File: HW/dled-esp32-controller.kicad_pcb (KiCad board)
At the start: 2 copper layers, 50 x 48 mm, 40 parts, among them J1 CS_4, J2 CS_3, J3 CS_2, J4 CS_2, J5 CS_3, J6 CS_5, J7 CS_3, J8 CS_Pwr, J9 CS_Pwr, Q1 STD46P4LLF6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

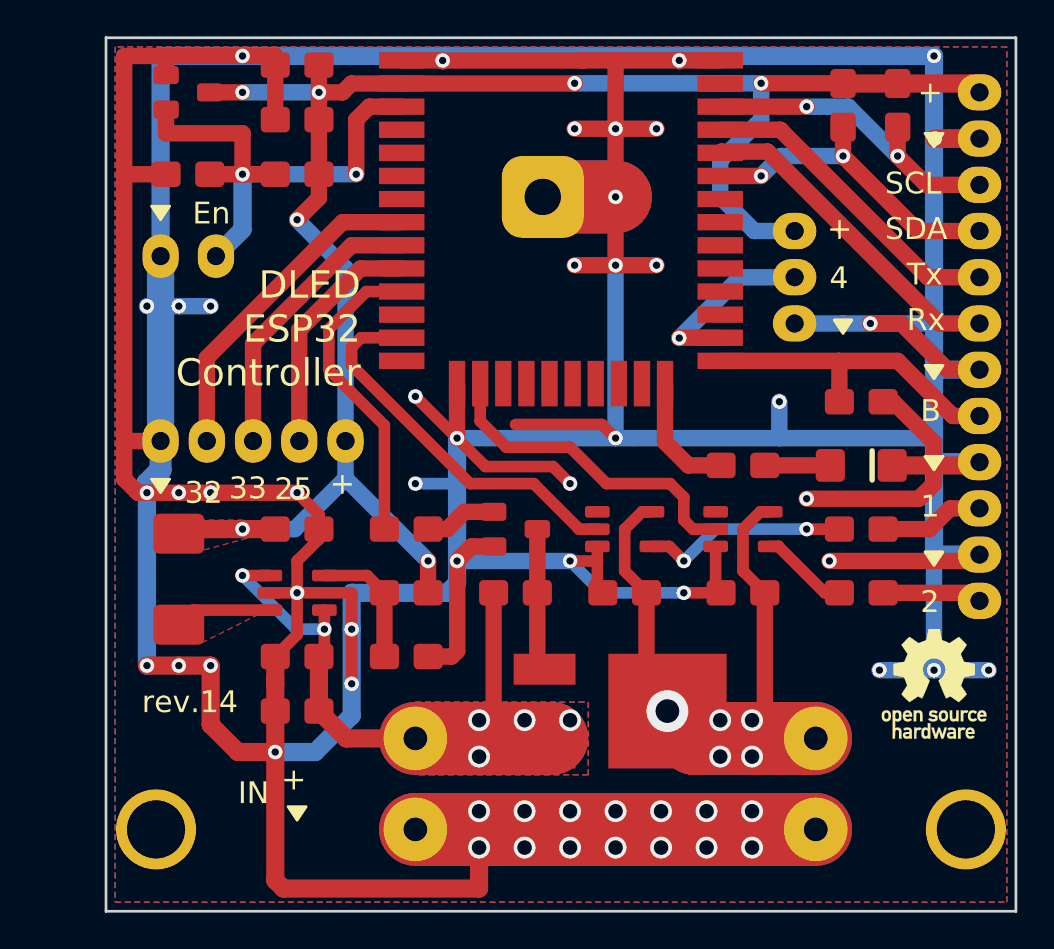
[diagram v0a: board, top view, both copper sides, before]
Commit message: Changes the C4 to NC and removes the keepout areas from under ESP32 module, as in Espressif's DevKitC v4
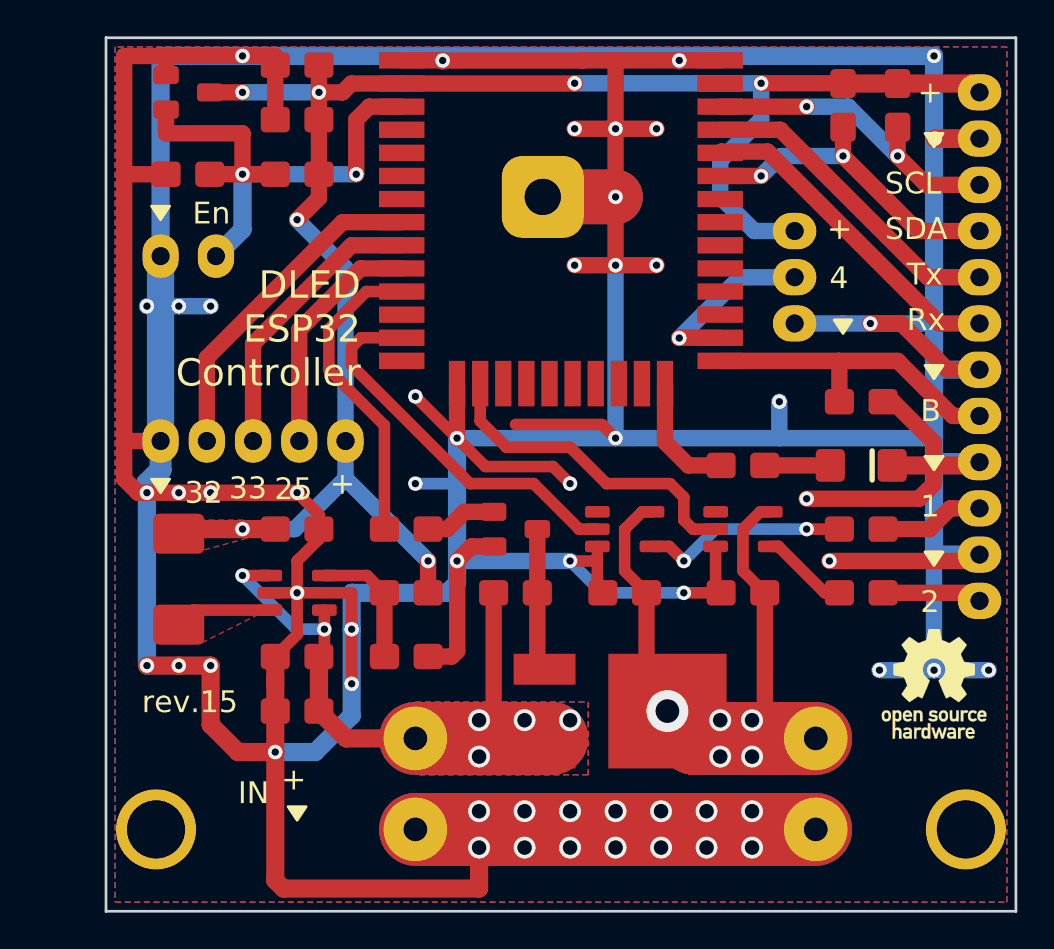
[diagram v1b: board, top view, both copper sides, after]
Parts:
- C4: value 100nF -> 100nF-NC
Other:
- board text added: "rev.15"
- board text removed: "rev.14"
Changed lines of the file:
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@@
       (effects (font (size 1 1) (thickness 0.15)))
     )
-    (fp_text value 100nF (at 0 -2) (layer F.Fab)
+    (fp_text value 100nF-NC (at 0 -2) (layer F.Fab)
       (effects (font (size 1 1) (thickness 0.15)))
     )
@@
     )
   )
-  (gr_text rev.14 (at 32.25 88.5) (layer F.SilkS)
+  (gr_text rev.15 (at 32.25 88.5) (layer F.SilkS)
     (effects (font (size 1.2 1.2) (thickness 0.25)) (justify right))
   )
@@
   (via (at 30.75 77) (size 0.8) (drill 0.4) (layers F.Cu B.Cu) (net 1))
   (segment (start 56.5 53.245) (end 53 53.245) (width 0.9) (layer F.Cu) (net 1))
-  (segment (start 49 60.745) (end 53 60.745) (width 4) (layer F.Cu) (net 1) (status 10))
-  (segment (start 49 60.745) (end 53 60.745) (width 4) (layer B.Cu) (net 1) (status 10))
+  (segment (start 49 60.745) (end 53 60.745) (width 3) (layer F.Cu) (net 1) (status 10))
+  (segment (start 49 60.745) (end 53 60.745) (width 3) (layer B.Cu) (net 1) (status 10))
   (via (at 53 60.745) (size 0.8) (drill 0.4) (layers F.Cu B.Cu) (net 1))
   (via (at 50.75 57) (size 0.8) (drill 0.4) (layers F.Cu B.Cu) (net 1))
@@
     )
   )
-  (zone (net 0) (net_name "") (layer F.Cu) (hatch edge 0.508)
-    (connect_pads no (clearance 0.8))
-    (min_thickness 0.5)
-    (keepout (tracks allowed) (vias allowed) (copperpour not_allowed))
-    (fill (arc_segments 16) (thermal_gap 0.5) (thermal_bridge_width 0.5))
-    (polygon
-      (pts
-        (xy 42.5 54.5) (xy 45 54.5) (xy 47 56.5) (xy 47 69) (xy 42.5 69)
-      )
-    )
-  )
   (zone (net 9) (net_name +5V) (layer F.Cu) (hatch edge 0.508)
     (priority 1)
@@
       )
     )
-  )
-  (zone (net 0) (net_name "") (layer B.Cu) (hatch edge 0.508)
-    (connect_pads no (clearance 0.8))
-    (min_thickness 0.5)
-    (keepout (tracks allowed) (vias allowed) (copperpour not_allowed))
-    (fill (arc_segments 16) (thermal_gap 0.5) (thermal_bridge_width 0.5))
-    (polygon
-      (pts
-        (xy 42.5 54.5) (xy 45 54.5) (xy 47 56.5) (xy 47 69) (xy 42.5 69)
-      )
-    )

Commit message: Improves component placement for ESP's power and reset circuitry.
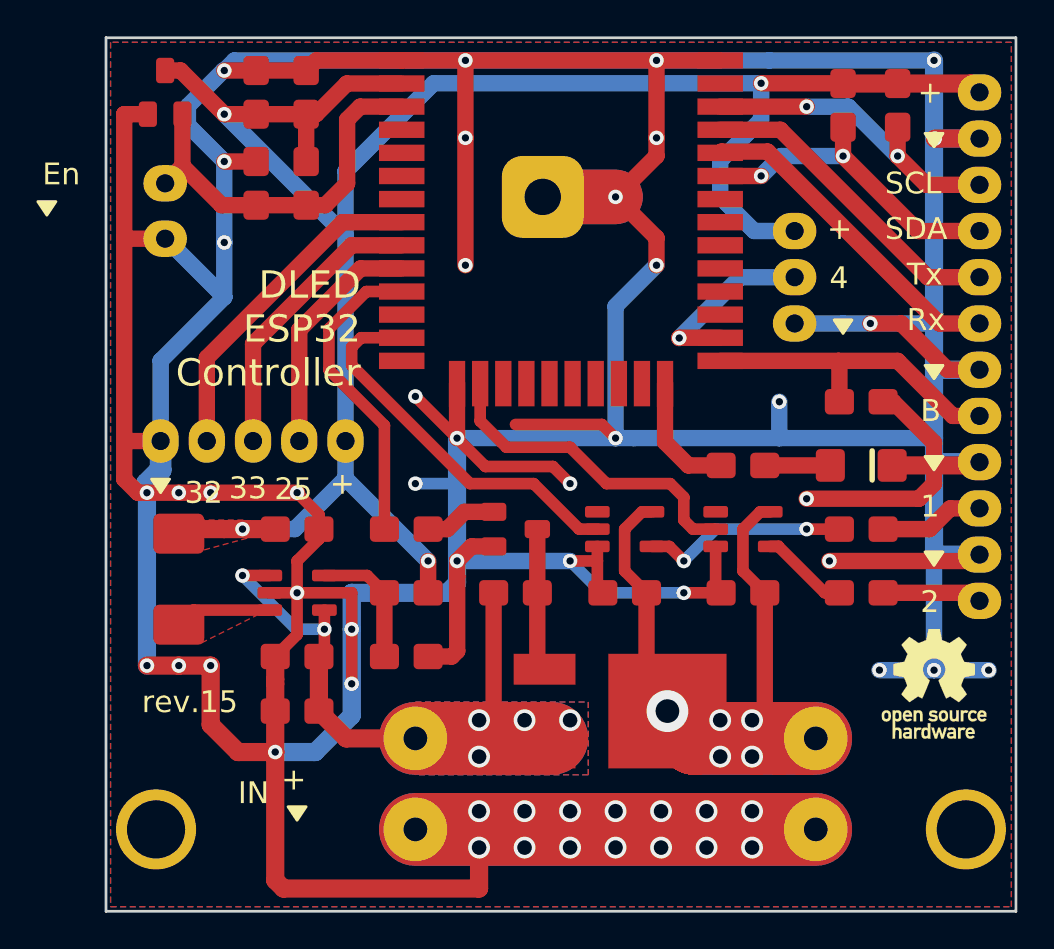
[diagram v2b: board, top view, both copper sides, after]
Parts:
- moved J4 4.88 mm to (28.2, 60.0), turned to 0 degrees
- moved C1 3.78 mm to (33.2, 60.0), turned to 90 degrees
- moved C3 2.70 mm to (33.2, 55.0), turned to 90 degrees
- moved C2 1.58 mm to (36.0, 55.0), turned to 90 degrees
- moved U2 1.25 mm to (28.2, 55.0), turned to 90 degrees
- moved R1 0.71 mm to (36.0, 60.0), turned to 270 degrees
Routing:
- net +3V3: track 99.5 -> 113.1 mm, vias 7 -> 4
- net /Reset: track 28.5 -> 21.4 mm, vias 2 -> 0
- net GND: track 486.9 -> 488.2 mm, vias 55 -> 52

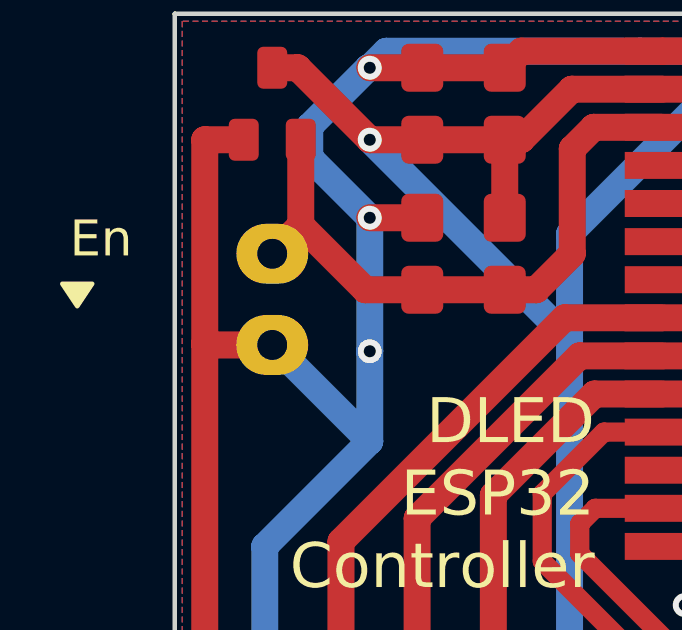
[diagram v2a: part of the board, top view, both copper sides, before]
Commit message: Creates the files for PCB fabrication, and adjusts the PCB layout a little.
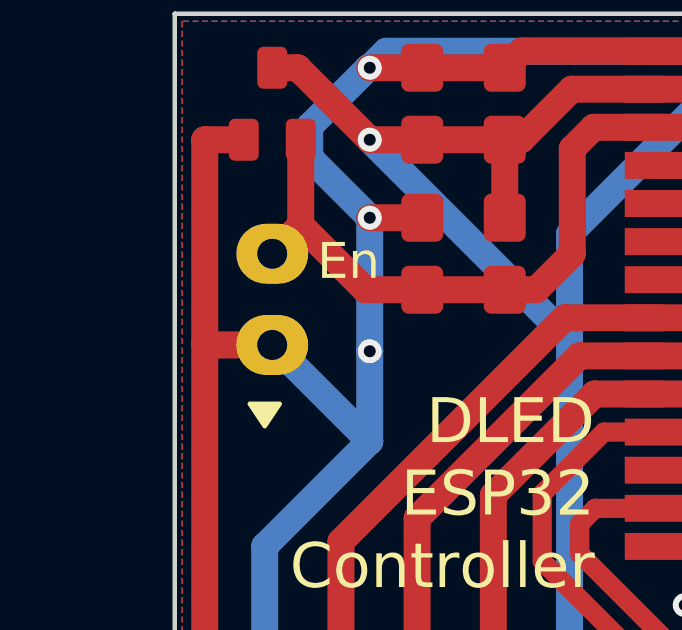
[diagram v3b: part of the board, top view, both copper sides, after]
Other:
- rule pad_to_mask_clearance: 0.051 -> 0.08
- rule solder_mask_min_width: 0.25 -> 0.35
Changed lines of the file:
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@@
   )
   (setup
-    (last_trace_width 0.9)
+    (last_trace_width 0.35)
     (user_trace_width 0.35)
     (user_trace_width 0.6)
@@
     (user_trace_width 4)
     (trace_clearance 0.3)
-    (zone_clearance 0.8)
+    (zone_clearance 0.7)
     (zone_45_only no)
     (trace_min 0.35)
@@
     (pad_size 3.5 3.5)
     (pad_drill 1.3)
-    (pad_to_mask_clearance 0.051)
-    (solder_mask_min_width 0.25)
+    (pad_to_mask_clearance 0.08)
+    (solder_mask_min_width 0.35)
     (aux_axis_origin 0 0)
     (visible_elements 7FFFFFFF)
     (pcbplotparams
-      (layerselection 0x010fc_ffffffff)
-      (usegerberextensions false)
+      (layerselection 0x010f0_ffffffff)
+      (usegerberextensions true)
       (usegerberattributes false)
       (usegerberadvancedattributes false)
@@
       (psnegative false)
       (psa4output false)
-      (plotreference true)
-      (plotvalue true)
+      (plotreference false)
+      (plotvalue false)
       (plotinvisibletext false)
-      (padsonsilk false)
+      (padsonsilk true)
       (subtractmaskfromsilk false)
       (outputformat 1)
       (mirror false)
-      (drillshape 1)
+      (drillshape 0)
       (scaleselection 1)
-      (outputdirectory ""))
+      (outputdirectory "Fab/"))
   )
   (net 0 "")
@@
   (gr_poly (pts (xy 70 80.25) (xy 71 80.25) (xy 70.5 81)) (layer F.SilkS) (width 0.15))
   (gr_poly (pts (xy 70 75) (xy 71 75) (xy 70.5 75.75)) (layer F.SilkS) (width 0.15))
-  (gr_poly (pts (xy 21.25 61) (xy 22.25 61) (xy 21.75 61.75)) (layer F.SilkS) (width 0.15))
-  (gr_text En (at 21.5 59.5) (layer F.SilkS)
+  (gr_poly (pts (xy 27.5 65) (xy 28.5 65) (xy 28 65.75)) (layer F.SilkS) (width 0.15))
+  (gr_text En (at 29.75 60.25) (layer F.SilkS)
     (effects (font (size 1.2 1.2) (thickness 0.25)) (justify left))
   )
@@
     (effects (font (size 1.2 1.2) (thickness 0.25)) (justify left))
   )
-  (gr_text "github.com\n   CalinRadoni\n      dled-esp32-controller" (at 55.75 69.25) (layer B.SilkS)
+  (gr_text "github.com\n   CalinRadoni\n      dled-esp32-controller" (at 55.75 68) (layer B.SilkS)
     (effects (font (size 1.3 1.3) (thickness 0.28)) (justify left mirror))
   )
-  (gr_text "designed with KiCad for hand soldering" (at 54.5 84.75) (layer B.SilkS)
+  (gr_text "designed with KiCad for hand soldering" (at 54.75 84.75) (layer B.SilkS)
     (effects (font (size 1 1) (thickness 0.2)) (justify mirror))
   )
@@
   (gr_line (start 75 100) (end 75 52) (layer Edge.Cuts) (width 0.15))
   (gr_line (start 25 100) (end 25 52) (layer Edge.Cuts) (width 0.15))
-  (via (at 31.5 56.2) (size 0.8) (drill 0.4) (layers F.Cu B.Cu) (net 3))
   (via (at 31.5 53.8) (size 0.8) (drill 0.4) (layers F.Cu B.Cu) (net 1))
   (via (at 44.29 74) (size 0.8) (drill 0.4) (layers F.Cu B.Cu) (net 1))
@@
   (segment (start 38.25 60) (end 38.25 56.5) (width 0.9) (layer F.Cu) (net 2))
   (segment (start 38.25 56.5) (end 38.965 55.785) (width 0.9) (layer F.Cu) (net 2))
+  (via (at 31.5 56.2) (size 0.8) (drill 0.4) (layers F.Cu B.Cu) (net 3))
   (segment (start 65.5 54.515) (end 68.5 54.515) (width 1) (layer F.Cu) (net 3) (status 30))
   (segment (start 72.515 54.515) (end 73 55) (width 1) (layer F.Cu) (net 3) (status 30))
@@
   (segment (start 31.5 79) (end 29.25 79) (width 1) (layer F.Cu) (net 3) (status 20))
   (segment (start 42.7 80.75) (end 42.7 82.5) (width 0.9) (layer F.Cu) (net 3) (status 20))
-  (via (at 61 54.5) (size 0.8) (drill 0.4) (layers F.Cu B.Cu) (net 3))
+  (via (at 61 54.5) (size 0.8) (drill 0.4) (layers F.Cu B.Cu) (net 3) (status 1000000))
   (segment (start 65.485 54.5) (end 65.5 54.515) (width 0.9) (layer F.Cu) (net 3) (status 30))
   (segment (start 61 54.5) (end 65.485 54.5) (width 0.9) (layer F.Cu) (net 3) (status 20))
@@
   (segment (start 56.5 68.5) (end 59.84 65.16) (width 0.9) (layer B.Cu) (net 27))
   (zone (net 1) (net_name GND) (layer B.Cu) (hatch edge 0.508)
-    (connect_pads no (clearance 0.8))
-    (min_thickness 0.8)
-    (fill yes (arc_segments 16) (thermal_gap 0.8) (thermal_bridge_width 0.8))
+    (connect_pads no (clearance 0.7))
+    (min_thickness 0.7)
+    (fill yes (arc_segments 32) (thermal_gap 0.7) (thermal_bridge_width 0.7))
     (polygon
       (pts
@@
   (zone (net 1) (net_name GND) (layer F.Cu) (hatch edge 0.508)
     (connect_pads no (clearance 0.7))
-    (min_thickness 1)
+    (min_thickness 0.7)
     (fill yes (arc_segments 32) (thermal_gap 0.7) (thermal_bridge_width 0.7))
     (polygon
